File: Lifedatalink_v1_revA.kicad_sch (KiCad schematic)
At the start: 91 parts, among them J1 DX07S024XJ1R1100, J10 503480-0400, J11 5034801400, J12 5034801400, J13 503480-0600, J14 503480-0600, J15 503480-0600, J16 503480-0600, J17 503480-0600, J18 ECG_RIGHT_LEG, J19 MOUNTING_HOLE_MAIN, J2 SM02B-SRSS-TB(LF)(SN), J20 MOUNTING_HOLE_ECG, J3 503480-0600, J4 Conn_01x06, J5 503480-0600, J6 ECG_LEFT_ARM, J7 ECG_RIGHT_ARM, J8 503480-0600, J9 503480-0400, Q1 CSD23280F3, SW1 SW_Push, U1 BL654, U2 LP5907MFX-3_3_NOPB, U3 ADS1292RIRSMT, U4 MCP73831T-2ACI/OT, U5 TMP117NAIYBGR, U6 MAX30102, U7 LP5907MFX-1.8/NOPB, U8 IIS2DLPCTR, U9 PCA9306DQER, Y1 Crystal

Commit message: Update schematic components
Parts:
- removed C17, C19, C23, C27: 100nF, Capacitor_SMD:C_0402_1005Metric, symbol Device:C
- removed C18, C20: 2.2nF, Capacitor_SMD:C_0402_1005Metric, symbol Device:C
- removed C21: 47pF, Capacitor_SMD:C_0402_1005Metric, symbol Device:C
- removed C22, C28: 10uF, Capacitor_SMD:C_0402_1005Metric, symbol Device:C
- removed D1: TPD4S012DRYR, SnapEda:SON50P100X145X60-6N, symbol dk_TVS-Diodes:TPD4S012DRYR
- removed D2: WS2812B, APA-102-2020-256-8:LED_WS2812-2020, symbol LED:WS2812B
- removed J10, J9: 503480-0400, 503480-0400:MOLEX_503480-0400, symbol 503480-0400:503480-0400
- removed J11, J12: 5034801400, MOLEX_503480-0600:5034801400, symbol Connector_Generic_Shielded:Conn_01x14_Shielded
- removed J13, J14, J15, J16, J17, J3, J5, J8: 503480-0600, MOLEX_503480-0600:MOLEX_503480-0600, symbol 503480-0600:503480-0600
- removed J18: ECG_RIGHT_LEG, MOLEX_503480-0600:ECG_SNAP, symbol Connector_Generic:Conn_01x01
- removed J2: SM02B-SRSS-TB(LF)(SN), Connector_JST:JST_SH_SM02B-SRSS-TB_1x02-1MP_P1.00mm_Horizontal, symbol Connector_Generic:Conn_01x02
- removed J6: ECG_LEFT_ARM, MOLEX_503480-0600:ECG_SNAP, symbol Connector_Generic:Conn_01x01
- removed J7: ECG_RIGHT_ARM, MOLEX_503480-0600:ECG_SNAP, symbol Connector_Generic:Conn_01x01
- removed R10, R9: 10M, Resistor_SMD:R_0402_1005Metric, symbol Device:R
- removed R11: 1M, Resistor_SMD:R_0402_1005Metric, symbol Device:R
- removed R12, R14: 100K, Resistor_SMD:R_0402_1005Metric, symbol Device:R
- removed R13: 0R, Resistor_SMD:R_0402_1005Metric, symbol Device:R
- removed R15, R16: 45.3K, Resistor_SMD:R_0402_1005Metric, symbol Device:R
- removed R19, R20, R21: 4.7K, Resistor_SMD:R_0402_1005Metric, symbol Device:R
- removed U1: BL654, XCVR_451-00001:XCVR_451-00001, symbol 451-00001:451-00001
- removed U2: LP5907MFX-3_3_NOPB, Package_TO_SOT_SMD:SOT-23-5, symbol dk_PMIC-Voltage-Regulators-Linear:LP5907MFX-3_3_NOPB
- removed U3: ADS1292RIRSMT, Package_DFN_QFN:QFN-32-1EP_4x4mm_P0.4mm_EP2.9x2.9mm, symbol Analog_ADC:ADS1292R
- removed U5: TMP117NAIYBGR, Package_BGA:Texas_DSBGA-6_0.9x1.4mm_Layout2x3_P0.5mm, symbol Sensor_Temperature:TMP117NAIYBGR
- removed U6: MAX30102, OptoDevice:Maxim_OLGA-14_3.3x5.6mm_P0.8mm, symbol Sensor:MAX30102
- removed U7: LP5907MFX-1.8/NOPB, Package_TO_SOT_SMD:SOT-23-5, symbol Regulator_Linear:LP5907MFX-1.8
- removed U8: IIS2DLPCTR, Package_LGA:LGA-12_2x2mm_P0.5mm, symbol IIS2DLPCTR:IIS2DLPCTR
- removed U9: PCA9306DQER, Package_SON:X2SON-8_1.4x1mm_P0.35mm, symbol Interface:PCA9306
- added C32: 0.1uF, Capacitor_SMD:C_0402_1005Metric, symbol Device:C
- added C33: 4.7uF, Capacitor_SMD:C_0402_1005Metric, symbol Device:C
- added C34, C35, C37: 1uF, Capacitor_SMD:C_0402_1005Metric, symbol Device:C
- added C36: 10uF, Capacitor_SMD:C_0402_1005Metric, symbol Device:C
- added C38, C39: 10pF, Capacitor_SMD:C_0402_1005Metric, symbol Device:C
- added J2: 5015680207, MOLEX_5015680207, symbol 5015680207:5015680207
- added U1: NORA-B106-00B, XCVR_NORA-B106-00B, symbol NORA-B106-00B:NORA-B106-00B
- added U10: TPD2E001IDRLRQ1, SOT50P160X60-5N, symbol TPD2E001IDRLRQ1:TPD2E001IDRLRQ1
- added U2: TCR3UG33A,LF, BGA4N35P2X2_64X64X33, symbol TCR3UG33A_LF:TCR3UG33A,LF
- added U3: ADS1293CISQE/NOPB, RSG28_3P6X3P6_TEX, symbol ADS1293CISQE:ADS1293CISQE/NOPB
- added U5: (no value), symbol LMT70AYFQT:LMT70AYFQT
- added U6: MAX86150EFF+T, XDCR_MAX86150EFF+, symbol MAX86150EFF_T:MAX86150EFF+T
- added U7: TCR3UG18A,LF, BGA4N35P2X2_64X64X33, symbol TCR3UG33A_LF:TCR3UG33A,LF
- added U8: LIS331DLHTR, LGA16R50P3X5_300X300X100, symbol LIS331DLHTR:LIS331DLHTR
- added U9: LTST-E263CEGBK, LTST-E263CEGBK_LTO, symbol LTST-E263CEGBK:LTST-E263CEGBK
- added Y2: Crystal, ABS05-32.768KHZ-T:ABS05-32.768KHZ-T, symbol Device:Crystal
- C10: value 100nF -> 22pF; footprint Capacitor_SMD:C_0402_1005Metric -> (none); MPN C0402C104K4PACTU -> (none)
- C11, C12: value 1uF -> 0.1uF; footprint Capacitor_SMD:C_0402_1005Metric -> (none); MPN C0402C105K9PACTU -> (none)
- C13: value 47nF -> 0.1uF; footprint Capacitor_SMD:C_0402_1005Metric -> (none); MPN C0402C473K3RACAUTO -> (none)
- C14: value 47nF -> 0.1uF; MPN C0402C473K3RACAUTO -> C0402C106M9PAC7867
- C15: value 2.2nF -> 10uF; MPN C0402C222K5RACTU -> C0402C106M9PAC7867
- C16: value 2.2nF -> (none); MPN C0402C222K5RACTU -> C0402C104K4PACTU
- C24: value 1uF -> 0.1uF
- C31: value 100pF -> 4.7uF; MPN C0402C101J5GACTU -> C0402C105K9PACTU
- C5: value 10uF -> 1.5nF; footprint Capacitor_SMD:C_0402_1005Metric -> (none); MPN C0402C106M9PAC7867 -> (none)
- C8: value 100nF -> 0.1uF; footprint Capacitor_SMD:C_0402_1005Metric -> (none); MPN C0402C104K4PACTU -> (none)
- C9: value 10uF -> 22pF; footprint Capacitor_SMD:C_0402_1005Metric -> (none); MPN C0402C106M9PAC7867 -> (none)
- D3: value MBR0540T1G -> SS0540_R1_00001; DK_Datasheet_Link http://www.onsemi.com/pub/Collateral/MBR0540T1-D.PDF -> (none); DK_Detail_Page /product-detail/en/on-semiconductor/MBR0540T1G/MBR0540T1GOS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 -> (none); Digi-Key_PN MBR0540T1GOSCT-ND -> 3757-SS0540_R1_00001CT-ND; MPN MBR0540T1G -> SS0540_R1_00001; Manufacturer ON Semiconductor -> Panjit International Inc.
- R17: value 200K -> R; footprint Resistor_SMD:R_0402_1005Metric -> (none); MPN RC0402FR-07200KL -> (none)
- R18: value 4.7K -> R; footprint Resistor_SMD:R_0402_1005Metric -> (none); MPN CRCW04024K70FKEDC -> (none)
- R3: value 10K -> 2K
- R5: value 10M -> 100K; footprint Resistor_SMD:R_0402_1005Metric -> (none); MPN CRCW040210M0FKED -> (none)
- R6: value 10M -> 1M; footprint Resistor_SMD:R_0402_1005Metric -> (none); MPN CRCW040210M0FKED -> (none)
- R7, R8: value 40.2K -> 1M; footprint Resistor_SMD:R_0402_1005Metric -> (none); MPN CRCW040240K2FKEDC -> (none)
- U4: value MCP73831T-2ACI/OT -> MCP73831T-3ACI/MC; footprint Package_TO_SOT_SMD:SOT-23-5 -> Package_DFN_QFN:DFN-8-1EP_3x2mm_P0.5mm_EP1.3x1.5mm; MPN MCP73831T-2ACI/OT -> MCP73831T-3ACI/MC
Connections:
- net +1V8: now also C24.2, C31.2, C32.2, C33.2, U6.13 (VDD_DIG), U6.14 (VDD_ANA), U7.A2 (VOUT); no longer R18.1
- net +3V3: now also C10.2, C11.2, C12.2, C14.2, C15.2, C16.2, C9.2, R7.2, R8.2, C36.2, C37.2, U1.A8 (VDDH), U1.B9 (VBUS), U2.A2 (VOUT), U3.22 (VDDIO), U3.28 (VDD), U5.A2 (VDD), U5.B2 (T_ON), U6.15 (VLED), U7.A1 (VIN), U7.B1 (CTRL), U8.1 (VDD_IO), U8.14 (VDD), U8.15 (RESERVED_2); no longer C24.2, C5.2, C8.2, R17.1, R5.2
- net +5V: now also U1.A7 (VDD), U1.B7 (VDD), U10.1 (VCC)
- net +BATT: now also J2.1
- net ACCEL_INT1: now also U1.F2 (P0.16/IO3), U8.11 (INT_1)
- net ACCEL_INT2: now also U1.F1 (P0.17/SCK), U8.9 (INT_2)
- net ADS_CLK: now also U1.G3 (P0.25/AIN4), U3.21 (CLK)
- net ADS_SPI_MISO: now also U1.H8 (P0.30)
- net ADS_SPI_MOSI: now also U1.H7 (P0.29)
- net ADS_SPI_SCLK: now also U1.J9 (P0.31)
- net ADS_START: now also U1.G2 (P0.26/AIN5)
- net GND: now also C13.1, C14.1, C15.1, C16.1, C8.2, C32.1, C33.1, C34.1, C36.1, C37.1, C38.1, C39.2, J2.2, U1.A1 (VSS), U1.A9 (VSS), U1.B2 (VSS), U1.B8 (VSS), U1.E4 (VSS), U1.E5 (VSS), U1.F4 (VSS), U1.F5 (VSS), U1.K2 (VSS), U1.K3 (VSS), U1.K5 (VSS), U1.K7 (VSS), U1.K8 (VSS), U1.L1 (VSS), U1.L9 (VSS), U1.M1 (VSS), U1.M2 (VSS), U1.M8 (VSS), U1.M9 (VSS), U10.4 (GND), U2.B2 (GND), U3.14 (VSSIO), U3.27 (VSS), U5.A1 (GND), U6.16 (PGND), U6.17 (GND_DIG), U6.18 (GND_ANA), U7.B2 (GND), U8.10 (RESERVED), U8.12 (GND_2), U8.13 (GND_4), U8.16 (GND), U8.5 (GND_3), U8.7 (SDO/SA0), U9.4 (VSS); no longer C10.1, C5.1, C8.1, C9.1, R6.2
- net MCP73831_STAT: now also U1.D2 (P0.13/IO0)
- net VIN: now also U2.A1 (VIN), U2.B1 (CTRL), U9.1 (VDD)
- net at C2.1, Y1.2: now also U1.B6 (P0.01/XL2)
- net at C1.1, Y1.1: now also U1.C6 (P0.00/XL1)
- net at SW1.1: now also U1.G8 (P1.12)
- net at C13.2: now also U3.26 (CVREF)
- net at R7.1: now also U3.13 (SYNCB)
- net at R8.1: now also U3.25 (RSTB)
- net at R17.2: now also C38.2, U6.4 (ECG_N); no longer C31.2
- net BL654_I2C_SDA_LV: no longer names the net of R18.2
- net BL654_I2C_SDA_LV: now also C39.1, U6.5 (ECG_P)
- net BL654_I2S_SCK_EXT renamed NORA_I2S_SCK_EXT
- net BL654_I2S_SD_EXT renamed NORA_I2S_SD_EXT
- net BL654_I2S_WS_EXT renamed NORA_I2S_WS_EXT
- net BL654_SWDCLK renamed NORA_SWDCLK
- net NORA_SWDCLK: now also U1.J2 (SWDCLK)
- net BL654_SWDIO renamed NORA_SWDIO
- net NORA_SWDIO: now also U1.H2 (SWDIO)
- net BL654_UART_RX renamed NORA_UART_RX
- net NORA_UART_RX: now also U1.A5 (P0.20)
- net BL654_UART_TX renamed NORA_UART_TX
- net NORA_UART_TX: now also U1.F3 (P0.19)
- net BL654_USB_DN renamed NORA_USB_DM
- net NORA_USB_DM: now also U1.D9 (USB_DM), U10.5 (IO2)
- net BL654_USB_DP renamed NORA_USB_DP
- net NORA_USB_DP: now also U1.C9 (USB_DP), U10.3 (IO1)
- net VDIV renamed BAT_VDIV
- net BAT_VDIV: now also U1.D8 (P0.04/AIN0)
- new net: U1.A6 (NC), U1.J1 (NC), U1.J4 (NC), U1.J5 (NC), U1.K1 (NC), U1.K9 (NC)
- new net: C34.2, U6.19 (VREF)
- new net: C35.2, U6.20 (C1_N)
- new net: C35.1, U6.21 (C1_P)
- new net: C5.1, R6.1, U3.9 (RLDOUT)
- new net: C5.2, R5.2, R6.2, U3.10 (RLDINV)
- new net: C10.1, U3.23 (XTAL1), Y2.2
- new net: C9.1, U3.24 (XTAL2), Y2.1
- new net: C8.1, U3.11 (RLDIN), U3.12 (RLDREF)
- new net: R5.1, U3.8 (CMOUT)
- new net ACCEL_CS: U1.D1 (P0.15/IO2), U8.8 (CS)
- new net ACCEL_SCL: U1.E2 (P0.14/IO1), U8.4 (SCL/SPC)
- new net ACCEL_SDA: U1.E1 (P0.18/CSN), U8.6 (SDA/SDI/SDO)
- new net ADS_ALARMB: U3.15 (ALARMB)
- new net ADS_CSB: U3.16 (CSB)
- new net ADS_DRDYB: U3.20 (DRDYB)
- new net ADS_SCLK: U3.17 (SCLK)
- new net ADS_SDI: U3.18 (SDI)
- new net ADS_SDO: U3.19 (SDO)
- new net ECG_N: R17.1, R18.1
- new net LED_DATA: U1.A4 (P1.00), U9.2 (DIN)
- new net NORA_I2C_SCL: U1.E9 (P1.05), U6.9 (SCL)
- new net NORA_I2C_SDA: U1.G1 (P1.06), U6.8 (SDA)
- new net NORA_I2S_SCK: U1.G5 (P1.08)
- new net NORA_I2S_SD: U1.G7 (P1.09)
- new net NORA_I2S_WS: U1.F7 (P1.07)
- new net TEMP_ADC_OUT: U5.B1 (TAO)
- new net ~{ADS_DRDY}: U1.H1 (P0.24)
- new net ~{ADS_PWDN_RESET}: U1.H3 (P0.27/AIN6)
- new net ~{ADS_SPI_CS}: U1.J8 (P0.28/AIN7)
- new net ~{MAX_INT}: U1.E3 (P0.21), U6.7 (INTB)
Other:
- note removed: "CHANNEL 1: RESPIRATION CHANNEL 2: ECG"
- note removed: "I2C LEVEL SHIFTER"
- note removed: "PPG SENSOR"
- note removed: "PPG SENSOR FPC"
- note removed: "RIGHT LEG FEEDBACK"
- note removed: "TEMP SENSOR FPC"
- title: LifeDataLink -> LifeDataLink-DevKit
- moved on the sheet: C25, C26, C29, C3, C30, C4, C6, C7, D3, F1, J1, J19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

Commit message: Update PCB form factor and place components
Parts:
- removed J19: MOUNTING_HOLE_MAIN, MountingHole:MountingHole_2.2mm_M2_DIN965_Pad, symbol Connector_Generic:Conn_01x01
- removed J20: MOUNTING_HOLE_ECG, MountingHole:MountingHole_2.2mm_M2_DIN965_Pad, symbol Connector_Generic:Conn_01x01
- removed J4: Conn_01x06, Pads_1.27mm:1.27mm_pads_01x06, symbol Connector_Generic:Conn_01x06
- added A1: Arduino_UNO_R3, Module:Arduino_UNO_R3, symbol MCU_Module:Arduino_UNO_R3
- added C17: 0.1uF, Capacitor_SMD:C_0402_1005Metric, symbol Device:C
- added J3, J5, J6: Conn_01x06, Pads_1.27mm:1.27mm_pads_01x06, symbol Connector_Generic:Conn_01x06
- added J4: Conn_01x02, Connector_PinHeader_2.54mm:PinHeader_1x02_P2.54mm_Vertical, symbol Connector_Generic:Conn_01x02
- added J7: ECG_IN, Connector_PinHeader_2.54mm:PinHeader_1x05_P2.54mm_Horizontal, symbol Connector_Generic:Conn_01x05
- added M1: MLX90614ESF-AAA-000-TU, Footprints:TO254P940H1340-4, symbol MLX90614ESF-AAA-000-TU:MLX90614ESF-AAA-000-TU
- C10, C11, C12, C13, C5, C8, C9: footprint (none) -> Capacitor_SMD:C_0402_1005Metric
- C16: value (none) -> 0.1uF
- J2: footprint MOLEX_5015680207 -> Footprints:MOLEX_5015680207
- MICL1: renamed from MIC1; footprint digikey-footprints:SPH0645LM4H-B -> Footprints:MIC_ICS-43434
- MICR1: renamed from MIC2; footprint digikey-footprints:SPH0645LM4H-B -> Footprints:MIC_ICS-43434
- R17, R18: value R -> 50K; footprint (none) -> Resistor_SMD:R_0402_1005Metric
- R5, R6, R7, R8: footprint (none) -> Resistor_SMD:R_0402_1005Metric
- U1: footprint XCVR_NORA-B106-00B -> Footprints:XCVR_NORA-B106-00B
- U10: footprint SOT50P160X60-5N -> Footprints:SOT50P160X60-5N
- U2, U7: footprint BGA4N35P2X2_64X64X33 -> Footprints:BGA4N35P2X2_64X64X33
- U3: footprint RSG28_3P6X3P6_TEX -> Footprints:ADS1293CISQE
- U5: value (none) -> LMT70AYFQT; footprint (none) -> Footprints:BGA4C40P2X2_88X88X68
- U6: footprint XDCR_MAX86150EFF+ -> Footprints:XDCR_MAX86150EFF+
- U8: footprint LGA16R50P3X5_300X300X100 -> Footprints:LGA16R50P3X5_300X300X100
- U9: footprint LTST-E263CEGBK_LTO -> Footprints:LTST-E263CEGBK
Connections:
- net NORA_I2S_SCK_EXT is gone; now on net NORA_I2S_SCK: MICL1.4 (BCLK), MICR1.4 (BCLK)
- net NORA_I2S_WS_EXT is gone; now on net NORA_I2S_WS: MICL1.1 (WS), MICR1.1 (WS)
- net ~{ADS_DRDY} is gone; now on net ADS_ALARMB: U1.H1 (P0.24)
- net +1V8: now also J6.6 (Pin_6)
- net +3V3: now also A1.4 (3V3), C17.2, J6.5 (Pin_5), M1.3 (VDD)
- net +5V: now also A1.5 (+5V)
- net +BATT: now also A1.8 (VIN)
- net ACCEL_CS: now also U1.A2 (P0.12/TRACECLK/DCX), J6.1 (Pin_1); no longer U1.D1 (P0.15/IO2)
- net ACCEL_INT1: now also U1.D2 (P0.13/IO0), J6.2 (Pin_2); no longer U1.F2 (P0.16/IO3)
- net ACCEL_INT2: now also U1.E2 (P0.14/IO1), J6.3 (Pin_3); no longer U1.F1 (P0.17/SCK)
- net ADS_ALARMB: now also J3.1 (Pin_1)
- net ADS_CLK: now also U1.E1 (P0.18/CSN); no longer U1.G3 (P0.25/AIN4)
- net ADS_CSB: now also U1.D7 (P0.23), J3.2 (Pin_2)
- net ADS_DRDYB: now also U1.F3 (P0.19), J3.6 (Pin_6)
- net ADS_SCLK: now also U1.C8 (P0.22), J3.3 (Pin_3)
- net ADS_SDI: now also U1.E3 (P0.21), J3.4 (Pin_4)
- net ADS_SDO: now also U1.A5 (P0.20), J3.5 (Pin_5)
- net GND: now also A1.29 (GND), A1.6 (GND), A1.7 (GND), C17.1, M1.4 (VSS)
- net LED_DATA: now also J5.6 (Pin_6)
- net MCP73831_STAT: now also U1.B3 (P0.11/TRACEDATA0/CSN), J6.4 (Pin_4); no longer U1.D2 (P0.13/IO0)
- net NORA_I2C_SCL: now also U8.4 (SCL/SPC), J5.1 (Pin_1)
- net NORA_I2C_SDA: now also U8.6 (SDA/SDI/SDO), J5.2 (Pin_2)
- net NORA_I2S_SCK: now also J5.4 (Pin_4)
- net NORA_I2S_SD: now also J5.5 (Pin_5)
- net NORA_I2S_WS: now also J5.3 (Pin_3)
- net NORA_SWDCLK: now also J4.1 (Pin_1)
- net NORA_SWDIO: now also J4.2 (Pin_2)
- net NORA_UART_RX: now also U1.F2 (P0.16/IO3), A1.15 (D0/RX); no longer U1.A5 (P0.20)
- net NORA_UART_TX: now also U1.D1 (P0.15/IO2), A1.16 (D1/TX); no longer U1.F3 (P0.19)
- net ~{MAX_INT}: now also U1.F1 (P0.17/SCK); no longer U1.E3 (P0.21)
- net at U3.1 (IN1): now also J7.5 (Pin_5)
- net at U3.2 (IN2): now also J7.4 (Pin_4)
- net at U3.3 (IN3): now also J7.3 (Pin_3)
- net at U3.4 (IN4): now also J7.2 (Pin_2)
- net at U3.5 (IN5): now also J7.1 (Pin_1)
- removed net ACCEL_SCL: U1.E2 (P0.14/IO1), U8.4 (SCL/SPC)
- removed net ACCEL_SDA: U1.E1 (P0.18/CSN), U8.6 (SDA/SDI/SDO)
- net ADS_SPI_MISO: no longer names the net of U1.H8 (P0.30)
- net ADS_SPI_MOSI: no longer names the net of U1.H7 (P0.29)
- net ADS_SPI_SCLK: no longer names the net of U1.J9 (P0.31)
- net ADS_START: no longer names the net of U1.G2 (P0.26/AIN5)
- net ~{ADS_PWDN_RESET}: no longer names the net of U1.H3 (P0.27/AIN6)
- net ~{ADS_SPI_CS}: no longer names the net of U1.J8 (P0.28/AIN7)
- new net MLX_SCL: M1.1 (SCL/VZ)
- new net MLX_SDA: M1.2 (SDA/PWM)
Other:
- moved on the sheet: C1, C10, C11, C12, C13, C14, C15, C16, C2, C5, C8, C9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

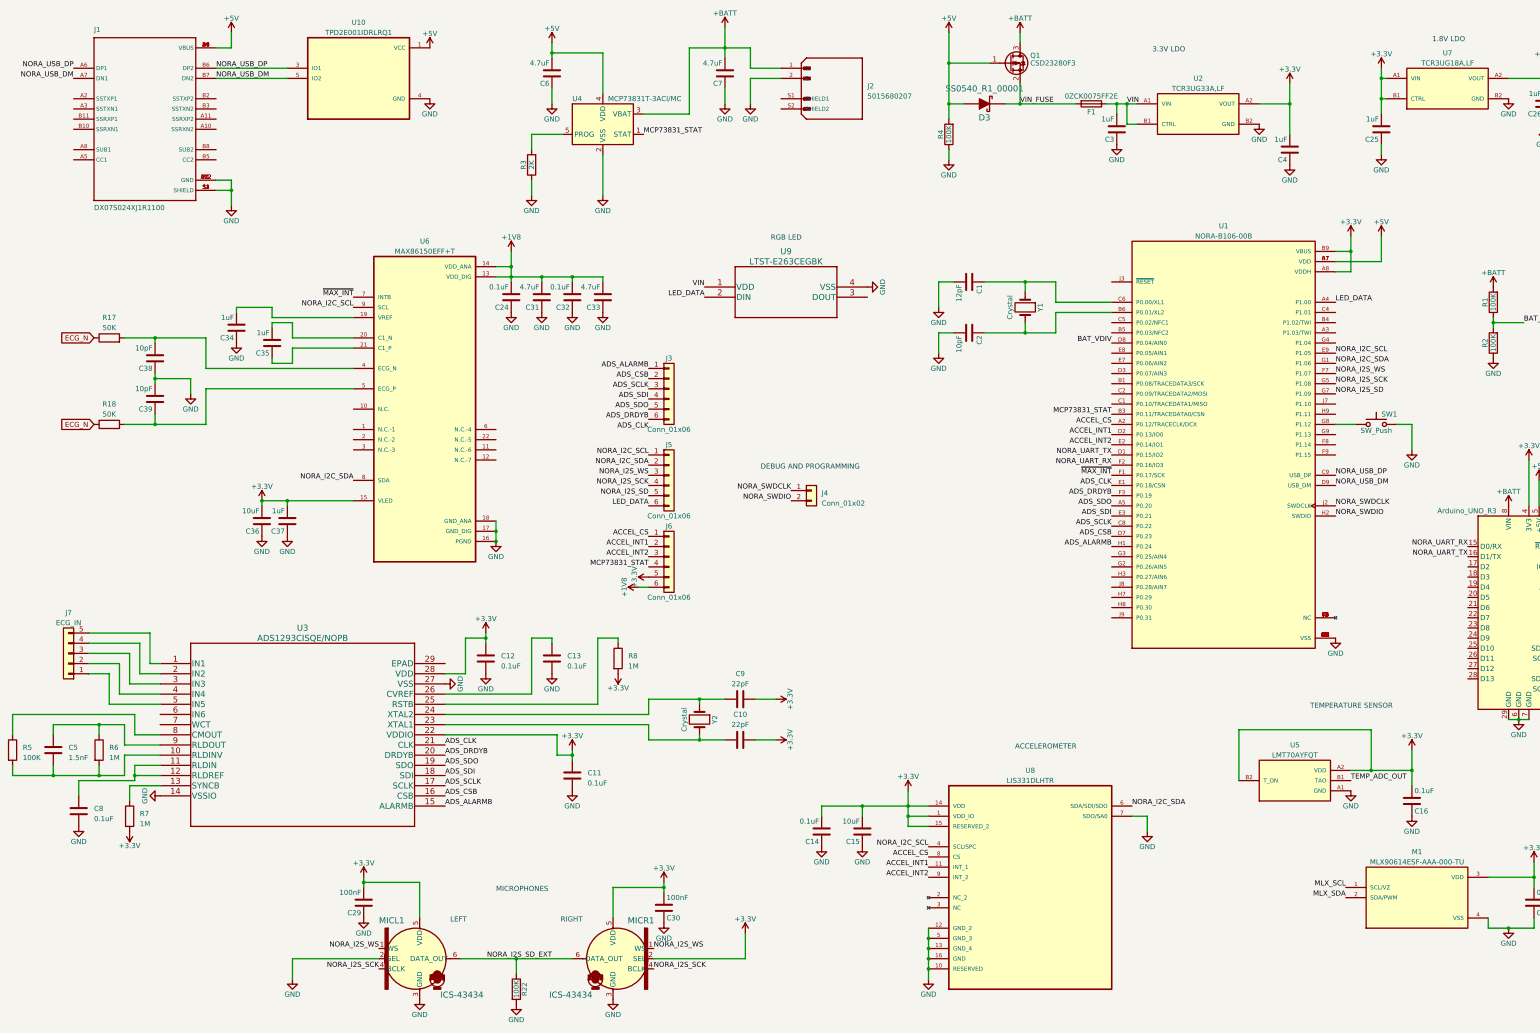
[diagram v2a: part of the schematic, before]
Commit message: Replace the BLE module with an ISP1807-LR-RS
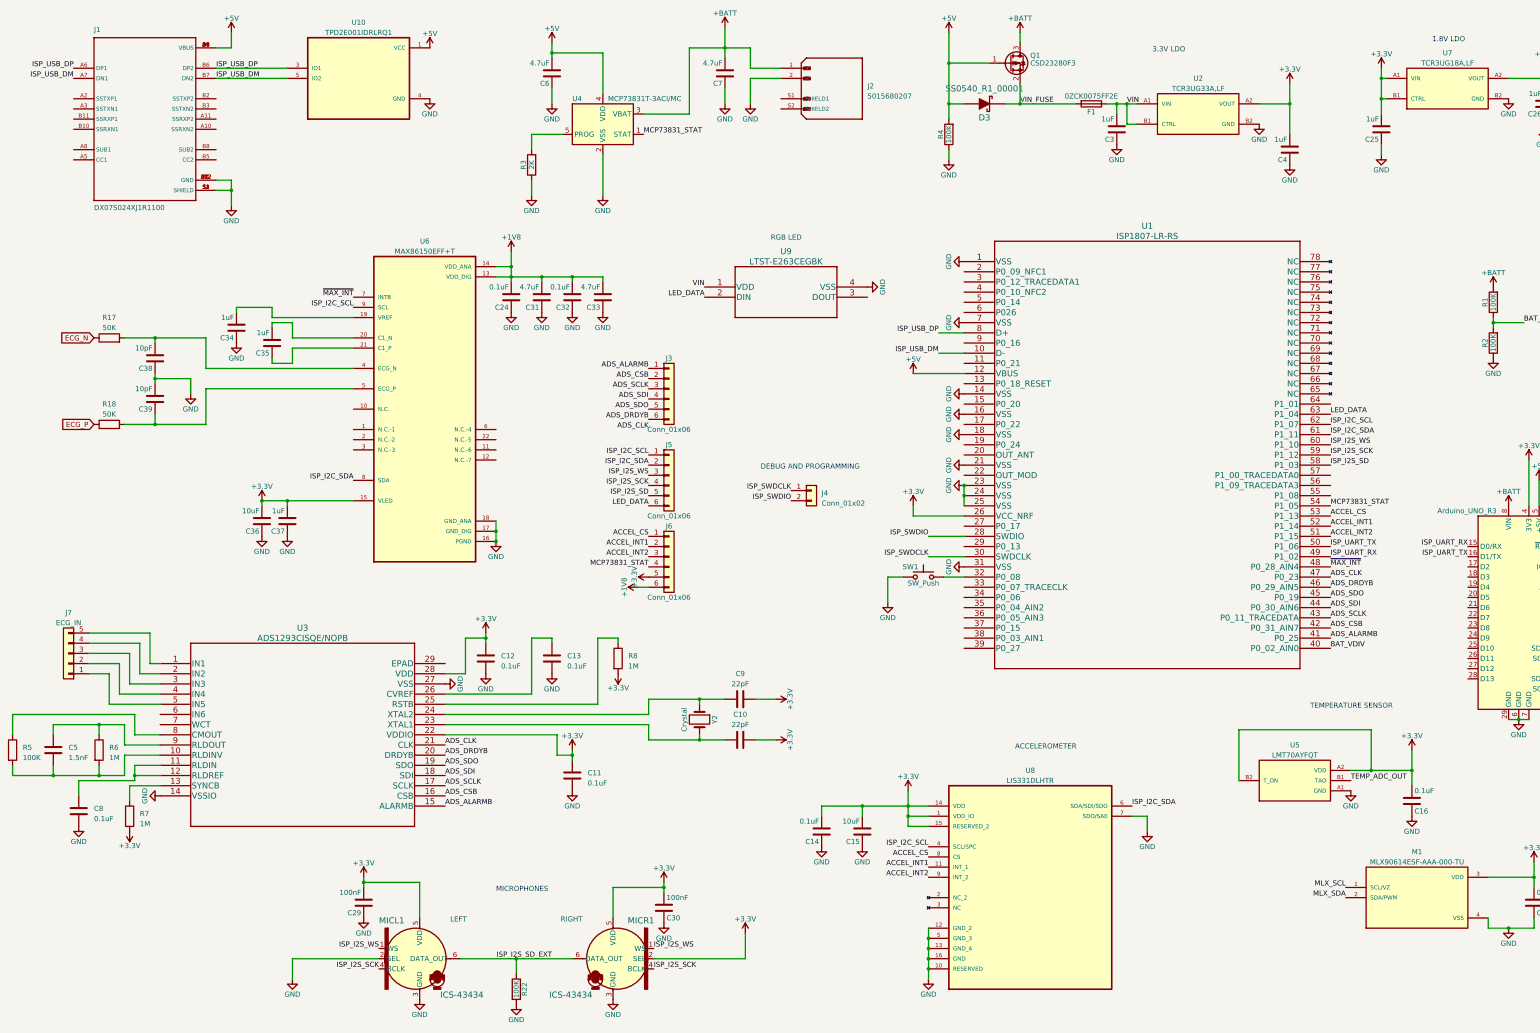
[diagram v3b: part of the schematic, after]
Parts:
- removed C1: 12pF, Capacitor_SMD:C_0402_1005Metric, symbol Device:C
- removed C2: 10pF, Capacitor_SMD:C_0402_1005Metric, symbol Device:C
- removed U1: NORA-B106-00B, Footprints:XCVR_NORA-B106-00B, symbol NORA-B106-00B:NORA-B106-00B
- removed Y1: Crystal, ABS05-32.768KHZ-T:ABS05-32.768KHZ-T, symbol Device:Crystal
- added U1: ISP1807-LR-RS, ISP1807-LR-RS, symbol ISP1807-LR-RS:ISP1807-LR-RS
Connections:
- net +3V3: now also U1.26 (VCC_NRF)
- net +5V: now also U1.12 (VBUS)
- net ACCEL_CS: now also U1.53 (P1_13)
- net ACCEL_INT1: now also U1.52 (P1_14)
- net ACCEL_INT2: now also U1.51 (P1_15)
- net ADS_ALARMB: now also U1.41 (P0_25)
- net ADS_CLK: now also U1.47 (P0_23)
- net ADS_CSB: now also U1.42 (P0_31_AIN7)
- net ADS_DRDYB: now also U1.46 (P0_29_AIN5)
- net ADS_SCLK: now also U1.43 (P0_11_TRACEDATA)
- net ADS_SDI: now also U1.44 (P0_30_AIN6)
- net ADS_SDO: now also U1.45 (P0_19)
- net BAT_VDIV: now also U1.40 (P0_02_AIN0)
- net ECG_N: no longer R18.1
- net GND: now also U1.1 (VSS), U1.14 (VSS), U1.16 (VSS), U1.18 (VSS), U1.21 (VSS), U1.23 (VSS), U1.24 (VSS), U1.25 (VSS), U1.31 (VSS), U1.7 (VSS)
- net LED_DATA: now also U1.63 (P1_04)
- net MCP73831_STAT: now also U1.54 (P1_05)
- net ~{MAX_INT}: now also U1.48 (P0_28_AIN4)
- net at SW1.1: now also U1.32 (P0_08)
- net NORA_I2C_SCL renamed ISP_I2C_SCL
- net ISP_I2C_SCL: now also U1.62 (P1_07)
- net NORA_I2C_SDA renamed ISP_I2C_SDA
- net ISP_I2C_SDA: now also U1.61 (P1_11)
- net NORA_I2S_SCK renamed ISP_I2S_SCK
- net ISP_I2S_SCK: now also U1.59 (P1_12)
- net NORA_I2S_SD renamed ISP_I2S_SD
- net ISP_I2S_SD: now also U1.58 (P1_03)
- net NORA_I2S_SD_EXT renamed ISP_I2S_SD_EXT
- net NORA_I2S_WS renamed ISP_I2S_WS
- net ISP_I2S_WS: now also U1.60 (P1_10)
- net NORA_SWDCLK renamed ISP_SWDCLK
- net ISP_SWDCLK: now also U1.30 (SWDCLK)
- net NORA_SWDIO renamed ISP_SWDIO
- net ISP_SWDIO: now also U1.28 (SWDIO)
- net NORA_UART_RX renamed ISP_UART_RX
- net ISP_UART_RX: now also U1.49 (P1_02)
- net NORA_UART_TX renamed ISP_UART_TX
- net ISP_UART_TX: now also U1.50 (P1_06)
- net NORA_USB_DM renamed ISP_USB_DM
- net ISP_USB_DM: now also U1.10 (D-)
- net NORA_USB_DP renamed ISP_USB_DP
- net ISP_USB_DP: now also U1.8 (D+)
- new net ECG_P: R18.1
